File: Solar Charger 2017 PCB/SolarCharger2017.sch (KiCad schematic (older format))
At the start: 23 parts, among them P1 5V OUT, P2 LiIon Cell V, P3 PV IN 1, P4 PV IN 2, P5 LiIon Cell V, P6 5V OUT, SW1 5V ON, U1 BQ24210

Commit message: Update of instructions
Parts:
- added P7: USB_A, Connectors:USB_A, symbol USB_A
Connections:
- net at DCDC1.3 (+Vout), DCDC2.3 (+Vout), P1.2 (P2)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: now also P7.1 (VBUS)
- net at DCDC1.4 (-Vout), DCDC2.4 (-Vout), P1.1 (P1)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: now also P7.4 (GND), P7.5 (shield)
- no-connect marks 4 -> 6
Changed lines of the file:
@@
 	4200 5800 4450 5800
 Connection ~ 4200 4900
+$Comp
+L USB_A P7
+U 1 1 5A036CD8
+P 6100 6600
+F 0 "P7" H 6300 6400 50  0000 C CNN
+F 1 "USB_A" H 6050 6800 50  0000 C CNN
+F 2 "Connectors:USB_A" V 6050 6500 50  0001 C CNN
+F 3 "" V 6050 6500 50  0000 C CNN
+	1    6100 6600
+	0    1    1    0
+$EndComp
+Wire Wire Line
+	5800 6400 5650 6400
+Wire Wire Line
+	5650 6400 5650 5800
+Connection ~ 5650 5800
+Wire Wire Line
+	5550 6050 5550 6700
+Wire Wire Line
+	5550 6700 5800 6700
+Connection ~ 5550 6050
+NoConn ~ 5800 6500
+NoConn ~ 5800 6600
+Wire Wire Line
+	6200 6900 6200 7000
+Wire Wire Line
+	6200 7000 5650 7000
+Wire Wire Line
+	5650 7000 5650 6700
+Connection ~ 5650 6700
 $EndSCHEMATC

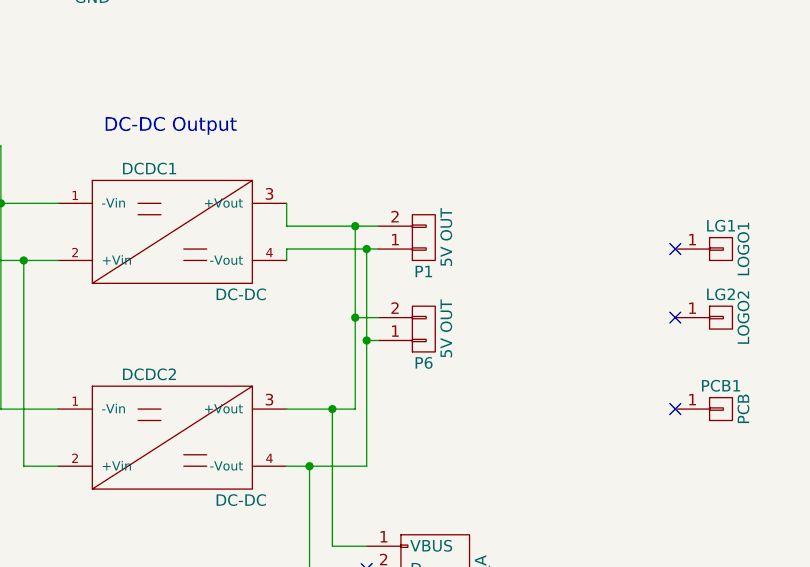
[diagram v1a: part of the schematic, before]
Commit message: Update of PCB with USB output
Slight change to the USB output.
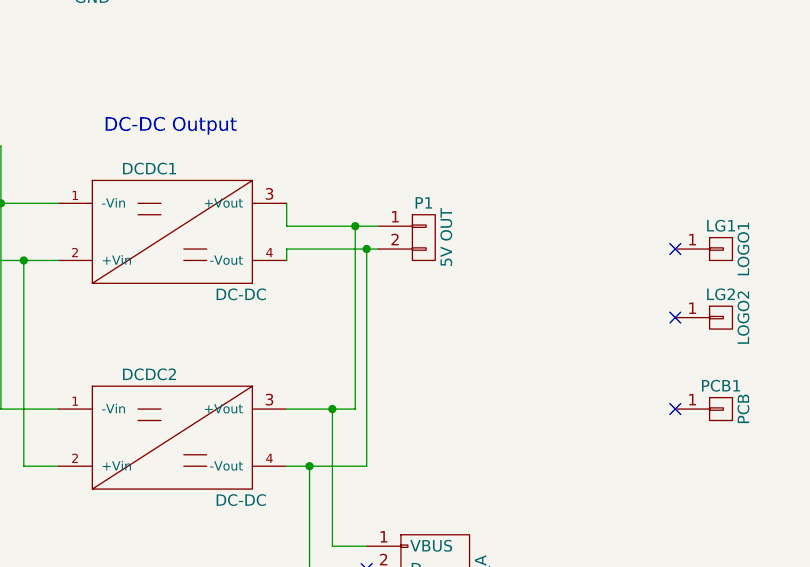
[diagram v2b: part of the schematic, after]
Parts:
- removed P6: 5V OUT, REInnovationFootprint:SIL-2_screw_terminal, symbol CONN_01X02
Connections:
- net at DCDC1.3 (+Vout), DCDC2.3 (+Vout), P7.1 (VBUS): now also P1.1 (P1); no longer P1.2 (P2)
- net at DCDC1.4 (-Vout), DCDC2.4 (-Vout), P7.4 (GND)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: now also P1.2 (P2); no longer P1.1 (P1)
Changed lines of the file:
@@
 F 3 "" H 6050 5050 50  0000 C CNN
 	1    6050 5050
-	1    0    0    1
+	1    0    0    -1
 $EndComp
 Wire Wire Line
@@
 Connection ~ 5800 5100
 $Comp
-L CONN_01X02 P6
-U 1 1 593EA27A
-P 6050 5450
-F 0 "P6" H 6050 5600 50  0000 C CNN
-F 1 "5V OUT" V 6150 5450 50  0000 C CNN
-F 2 "REInnovationFootprint:SIL-2_screw_terminal" H 6050 5450 50  0001 C CNN
-F 3 "" H 6050 5450 50  0000 C CNN
-	1    6050 5450
-	1    0    0    1
-$EndComp
-$Comp
 L CONN_01X02 P5
 U 1 1 593EA2E6
@@
 Connection ~ 8750 3100
 Wire Wire Line
-	5850 5400 5750 5400
-Connection ~ 5750 5400
-Wire Wire Line
-	5850 5500 5800 5500
-Connection ~ 5800 5500
-Wire Wire Line
 	4450 4900 4200 4900
